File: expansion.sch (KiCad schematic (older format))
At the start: 3 parts, among them J7 DF40HC(3.5)-60DS, J9 DF40HC(3.5)-60DS, U1 IMX8MM

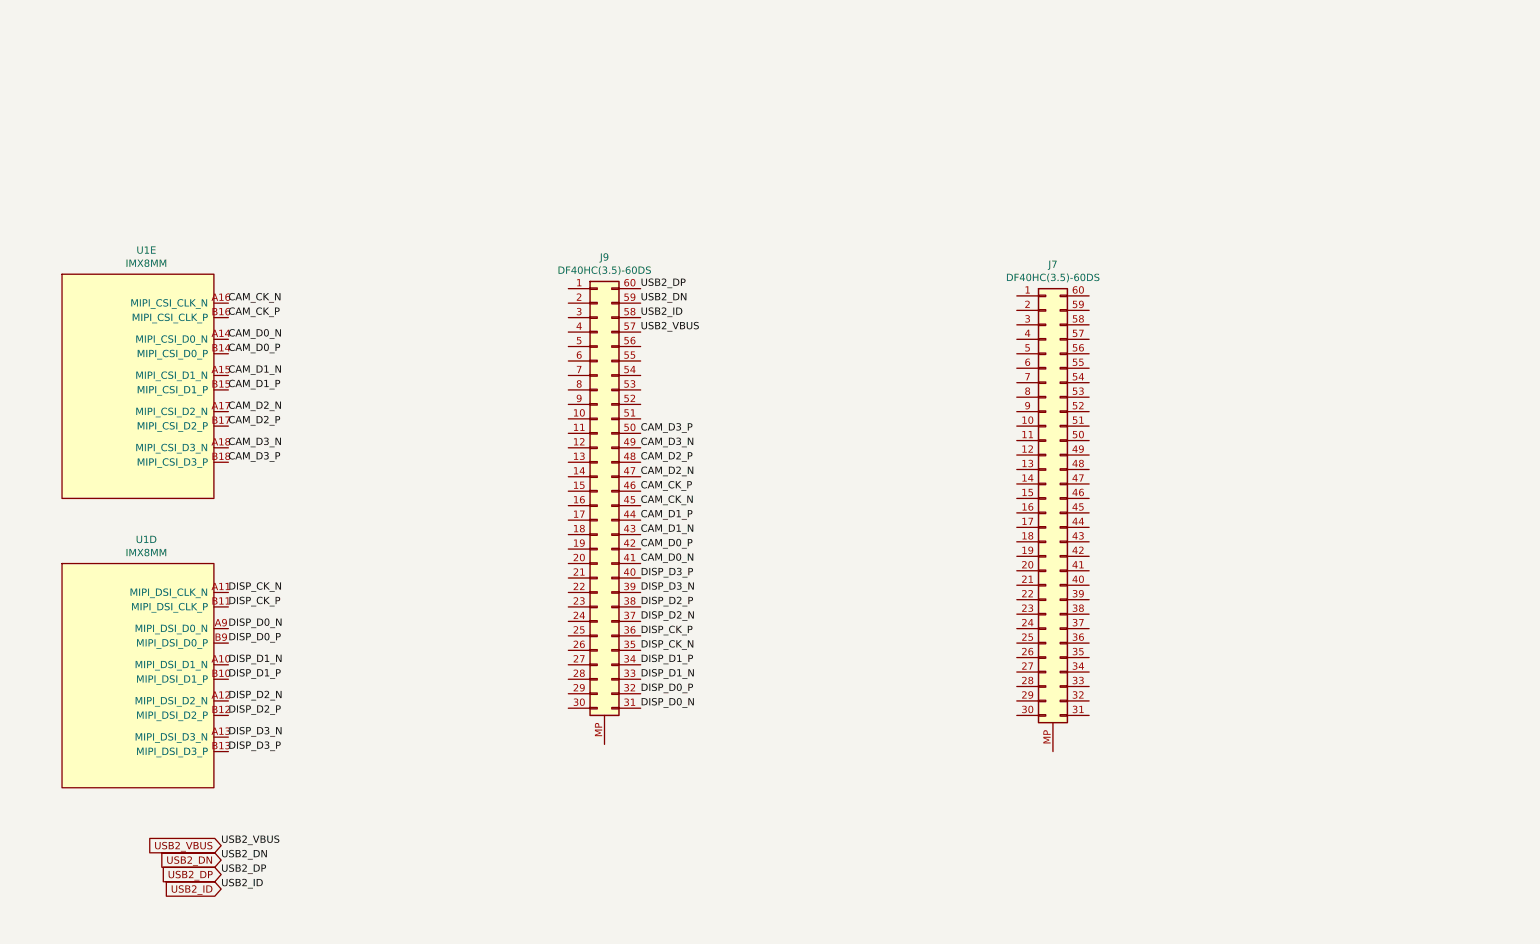
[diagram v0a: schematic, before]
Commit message: More new layout, buttons, and routing
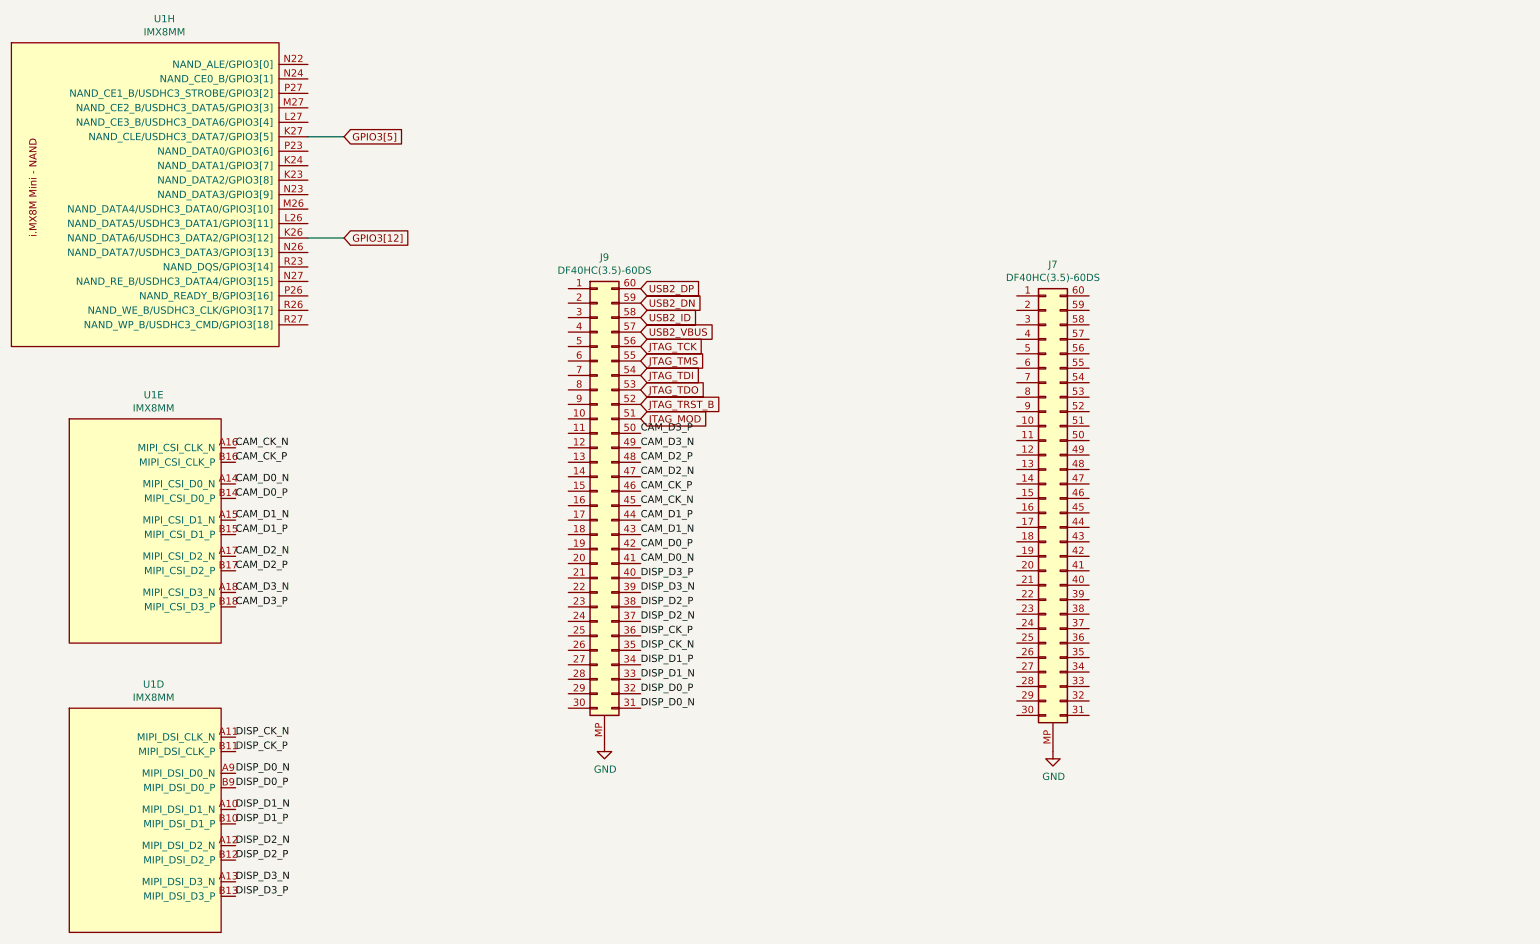
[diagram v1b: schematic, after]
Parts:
- added unit 8 of U1
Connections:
- net JTAG_MOD: now reaches J9.51 (Pin_51)
- net JTAG_TRST_B: now reaches J9.52 (Pin_52)
- net JTAG_TDO: now reaches J9.53 (Pin_53)
- net JTAG_TDI: now reaches J9.54 (Pin_54)
- net JTAG_TMS: now reaches J9.55 (Pin_55)
- net JTAG_TCK: now reaches J9.56 (Pin_56)
- net GND: now reaches J9.MP
- net GND: now also J7.MP
- new net GPIO3[12]: U1.K26 (NAND_DATA6/USDHC3_DATA2/GPIO3[12])
- new net GPIO3[5]: U1.K27 (NAND_CLE/USDHC3_DATA7/GPIO3[5])
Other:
- moved on the sheet: U1D, U1E
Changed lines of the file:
@@
 	1    0    0    -1
 $EndComp
-Text Label 2200 2650 0    50   ~ 0
+Text Label 2250 3650 0    50   ~ 0
 CAM_CK_N
-Text Label 2200 2750 0    50   ~ 0
+Text Label 2250 3750 0    50   ~ 0
 CAM_CK_P
-Text Label 2200 2900 0    50   ~ 0
+Text Label 2250 3900 0    50   ~ 0
 CAM_D0_N
-Text Label 2200 3000 0    50   ~ 0
+Text Label 2250 4000 0    50   ~ 0
 CAM_D0_P
-Text Label 2200 3150 0    50   ~ 0
+Text Label 2250 4150 0    50   ~ 0
 CAM_D1_N
-Text Label 2200 3250 0    50   ~ 0
+Text Label 2250 4250 0    50   ~ 0
 CAM_D1_P
 $Comp
 L mxenc:MIMX8MM6DVTLZAA U?
 U 5 1 5E38B0F0
-P 1600 5150
+P 1650 6150
 AR Path="/5DFA108C/5E38B0F0" Ref="U?"  Part="5"
 AR Path="/5E34BAA5/5E38B0F0" Ref="U1"  Part="5"
-F 0 "U1" H 1633 8015 50  0000 C CNN
-F 1 "IMX8MM" H 1633 7924 50  0000 C CNN
-F 2 "mxenc:BGA-729_27x27_14.0x14.0mm" H 1850 7900 50  0001 C CNN
-F 3 "" H 850 7900 50  0001 C CNN
-F 4 "NXP" H 1600 5150 50  0001 C CNN "Mfgr"
-F 5 "MIMX8MM6CVTKZAA" H 1600 5150 50  0001 C CNN "Part"
-F 6 "568-15276-ND" H 1600 5150 50  0001 C CNN "Vendorpart"
-	5    1600 5150
+F 0 "U1" H 1683 9015 50  0000 C CNN
+F 1 "IMX8MM" H 1683 8924 50  0000 C CNN
+F 2 "mxenc:BGA-729_27x27_14.0x14.0mm" H 1900 8900 50  0001 C CNN
+F 3 "" H 900 8900 50  0001 C CNN
+F 4 "NXP" H 1650 6150 50  0001 C CNN "Mfgr"
+F 5 "MIMX8MM6CVTKZAA" H 1650 6150 50  0001 C CNN "Part"
+F 6 "568-15276-ND" H 1650 6150 50  0001 C CNN "Vendorpart"
+	5    1650 6150
 	1    0    0    -1
 $EndComp
-Text Label 2200 3400 0    50   ~ 0
+Text Label 2250 4400 0    50   ~ 0
 CAM_D2_N
-Text Label 2200 3500 0    50   ~ 0
+Text Label 2250 4500 0    50   ~ 0
 CAM_D2_P
-Text Label 2200 3650 0    50   ~ 0
+Text Label 2250 4650 0    50   ~ 0
 CAM_D3_N
-Text Label 2200 3750 0    50   ~ 0
+Text Label 2250 4750 0    50   ~ 0
 CAM_D3_P
 Text Label 5050 4050 0    50   ~ 0
@@
 L mxenc:MIMX8MM6DVTLZAA U?
 U 4 1 5E3AB6A2
-P 1600 7150
+P 1650 8150
 AR Path="/5D6742B7/5E3AB6A2" Ref="U?"  Part="4"
 AR Path="/5E34BAA5/5E3AB6A2" Ref="U1"  Part="4"
-F 0 "U1" H 1633 10015 50  0000 C CNN
-F 1 "IMX8MM" H 1633 9924 50  0000 C CNN
-F 2 "mxenc:BGA-729_27x27_14.0x14.0mm" H 1850 9900 50  0001 C CNN
-F 3 "" H 850 9900 50  0001 C CNN
-F 4 "NXP" H 1600 7150 50  0001 C CNN "Mfgr"
-F 5 "MIMX8MM6CVTKZAA" H 1600 7150 50  0001 C CNN "Part"
-F 6 "568-15276-ND" H 1600 7150 50  0001 C CNN "Vendorpart"
-	4    1600 7150
+F 0 "U1" H 1683 11015 50  0000 C CNN
+F 1 "IMX8MM" H 1683 10924 50  0000 C CNN
+F 2 "mxenc:BGA-729_27x27_14.0x14.0mm" H 1900 10900 50  0001 C CNN
+F 3 "" H 900 10900 50  0001 C CNN
+F 4 "NXP" H 1650 8150 50  0001 C CNN "Mfgr"
+F 5 "MIMX8MM6CVTKZAA" H 1650 8150 50  0001 C CNN "Part"
+F 6 "568-15276-ND" H 1650 8150 50  0001 C CNN "Vendorpart"
+	4    1650 8150
 	1    0    0    -1
 $EndComp
-Text Label 2200 4650 0    50   ~ 0
+Text Label 2250 5650 0    50   ~ 0
 DISP_CK_N
-Text Label 2200 4750 0    50   ~ 0
+Text Label 2250 5750 0    50   ~ 0
 DISP_CK_P
-Text Label 2200 4900 0    50   ~ 0
+Text Label 2250 5900 0    50   ~ 0
 DISP_D0_N
-Text Label 2200 5000 0    50   ~ 0
+Text Label 2250 6000 0    50   ~ 0
 DISP_D0_P
-Text Label 2200 5150 0    50   ~ 0
+Text Label 2250 6150 0    50   ~ 0
 DISP_D1_N
-Text Label 2200 5250 0    50   ~ 0
+Text Label 2250 6250 0    50   ~ 0
 DISP_D1_P
-Text Label 2200 5400 0    50   ~ 0
+Text Label 2250 6400 0    50   ~ 0
 DISP_D2_N
-Text Label 2200 5500 0    50   ~ 0
+Text Label 2250 6500 0    50   ~ 0
 DISP_D2_P
-Text Label 2200 5650 0    50   ~ 0
+Text Label 2250 6650 0    50   ~ 0
 DISP_D3_N
-Text Label 2200 5750 0    50   ~ 0
+Text Label 2250 6750 0    50   ~ 0
 DISP_D3_P
 Text Label 5050 5050 0    50   ~ 0
@@
 Text Label 5050 4550 0    50   ~ 0
 DISP_D3_P
-Text Label 2150 6400 0    50   ~ 0
+Text GLabel 5050 2850 2    50   Input ~ 0
 USB2_VBUS
-Text Label 2150 6500 0    50   ~ 0
+Text GLabel 5050 2650 2    50   Input ~ 0
 USB2_DN
-Text Label 2150 6600 0    50   ~ 0
+Text GLabel 5050 2550 2    50   Input ~ 0
 USB2_DP
-Text Label 2150 6700 0    50   ~ 0
+Text GLabel 5050 2750 2    50   Input ~ 0
 USB2_ID
-Text GLabel 2150 6400 0    50   Input ~ 0
-USB2_VBUS
-Text GLabel 2150 6500 0    50   Input ~ 0
-USB2_DN
-Text GLabel 2150 6600 0    50   Input ~ 0
-USB2_DP
-Text GLabel 2150 6700 0    50   Input ~ 0
-USB2_ID
-Text Label 5050 2650 0    50   ~ 0
-USB2_DN
-Text Label 5050 2550 0    50   ~ 0
-USB2_DP
-Text Label 5050 2850 0    50   ~ 0
-USB2_VBUS
-Text Label 5050 2750 0    50   ~ 0
-USB2_ID
+$Comp
+L power:GND #PWR0151
+U 1 1 5E62C901
+P 4800 5700
+F 0 "#PWR0151" H 4800 5450 50  0001 C CNN
+F 1 "GND" H 4805 5527 50  0000 C CNN
+F 2 "" H 4800 5700 50  0001 C CNN
+F 3 "" H 4800 5700 50  0001 C CNN
+	1    4800 5700
+	1    0    0    -1
+$EndComp
+$Comp
+L power:GND #PWR0152
+U 1 1 5E62D325
+P 7900 5750
+F 0 "#PWR0152" H 7900 5500 50  0001 C CNN
+F 1 "GND" H 7905 5577 50  0000 C CNN
+F 2 "" H 7900 5750 50  0001 C CNN
+F 3 "" H 7900 5750 50  0001 C CNN
+	1    7900 5750
+	1    0    0    -1
+$EndComp
+Text GLabel 5050 2950 2    50   Input ~ 0
+JTAG_TCK
+Text GLabel 5050 3050 2    50   Input ~ 0
+JTAG_TMS
+Text GLabel 5050 3150 2    50   Input ~ 0
+JTAG_TDI
+Text GLabel 5050 3250 2    50   Input ~ 0
+JTAG_TDO
+Text GLabel 5050 3350 2    50   Input ~ 0
+JTAG_TRST_B
+Text GLabel 5050 3450 2    50   Input ~ 0
+JTAG_MOD
+$Comp
+L mxenc:MIMX8MM6DVTLZAA U1
+U 8 1 5E66E0E3
+P 1650 3550
+F 0 "U1" H 1758 6415 50  0000 C CNN
+F 1 "IMX8MM" H 1758 6324 50  0000 C CNN
+F 2 "mxenc:BGA-729_27x27_14.0x14.0mm" H 1900 6300 50  0001 C CNN
+F 3 "" H 900 6300 50  0001 C CNN
+	8    1650 3550
+	1    0    0    -1
+$EndComp
+Text GLabel 3000 2200 2    50   Input ~ 0
+GPIO3[12]
+Wire Wire Line
+	3000 2200 2750 2200
+Wire Wire Line
+	3000 1500 2750 1500
+Text GLabel 3000 1500 2    50   Input ~ 0
+GPIO3[5]
 $EndSCHEMATC

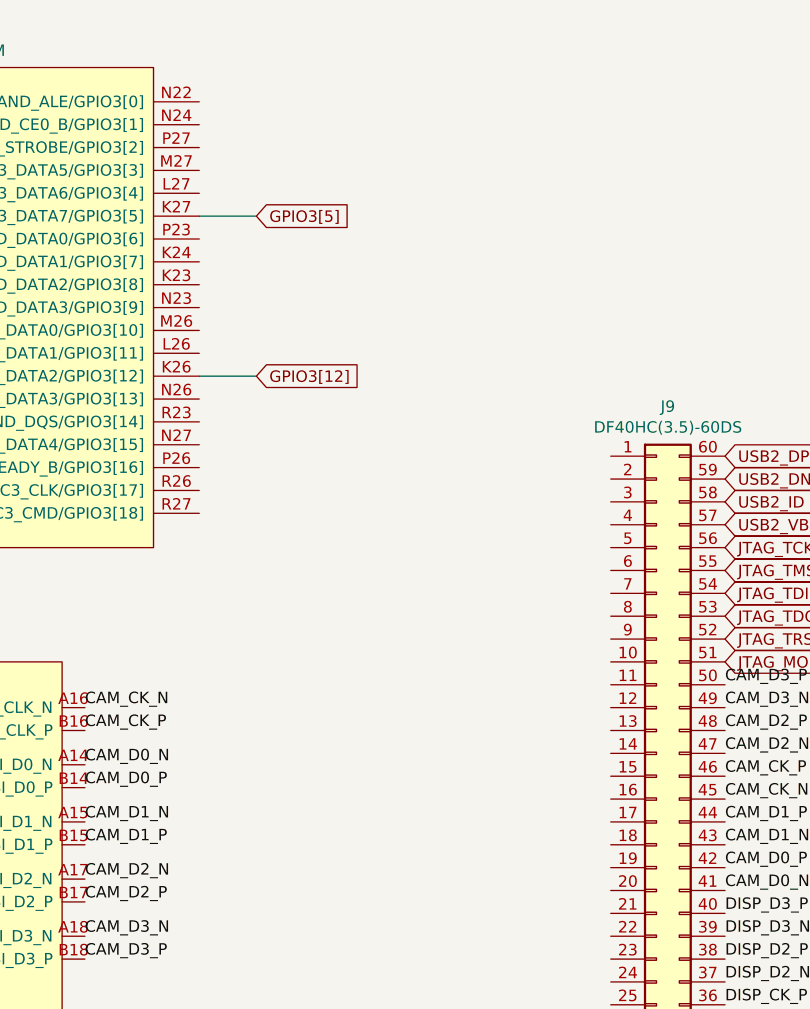
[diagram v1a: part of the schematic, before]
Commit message: rerouted sd, added some gpio, started power input
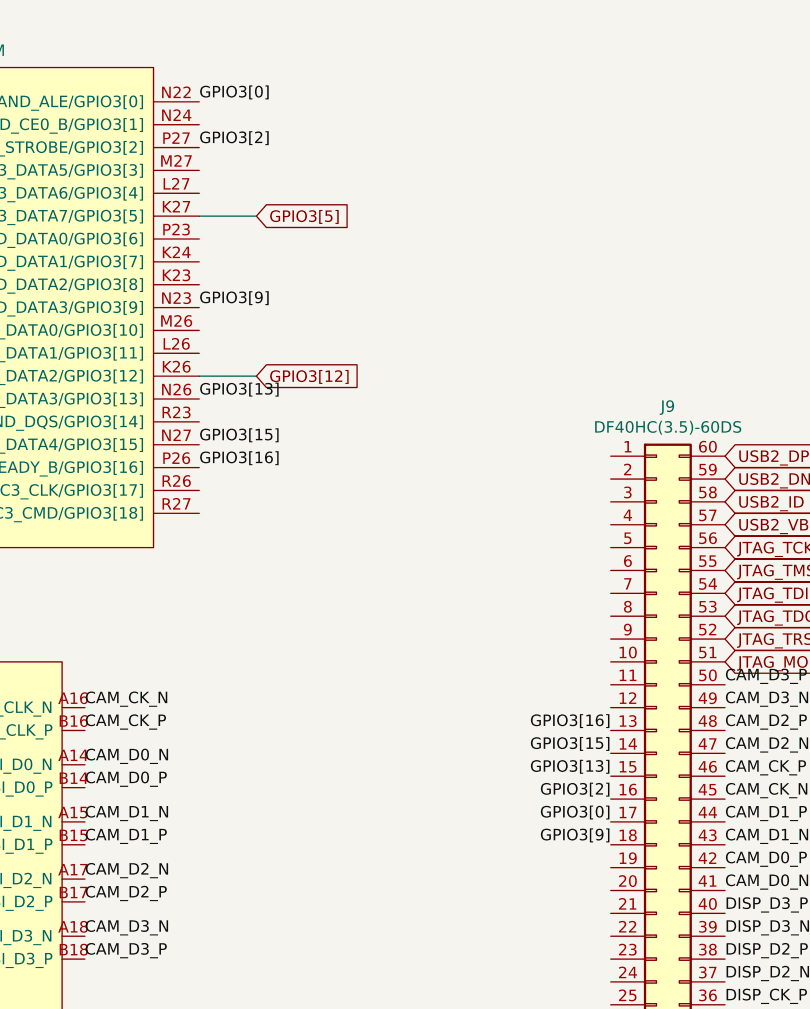
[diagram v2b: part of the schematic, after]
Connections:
- net GPIO3[16]: now reaches J9.13 (Pin_13)
- net GPIO3[16]: now also U1.P26 (NAND_READY_B/GPIO3[16])
- net GPIO3[15]: now reaches J9.14 (Pin_14)
- net GPIO3[15]: now also U1.N27 (NAND_RE_B/USDHC3_DATA4/GPIO3[15])
- net GPIO3[13]: now reaches J9.15 (Pin_15)
- net GPIO3[13]: now also U1.N26 (NAND_DATA7/USDHC3_DATA3/GPIO3[13])
- net GPIO3[2]: now reaches J9.16 (Pin_16)
- net GPIO3[2]: now also U1.P27 (NAND_CE1_B/USDHC3_STROBE/GPIO3[2])
- net GPIO3[0]: now reaches J9.17 (Pin_17)
- net GPIO3[0]: now also U1.N22 (NAND_ALE/GPIO3[0])
- net GPIO3[9]: now reaches J9.18 (Pin_18)
- net GPIO3[9]: now also U1.N23 (NAND_DATA3/GPIO3[9])
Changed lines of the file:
@@
 Text GLabel 3000 1500 2    50   Input ~ 0
 GPIO3[5]
+Text Label 2750 2300 0    50   ~ 0
+GPIO3[13]
+Text Label 2750 2500 0    50   ~ 0
+GPIO3[15]
+Text Label 2750 2600 0    50   ~ 0
+GPIO3[16]
+Text Label 2750 1200 0    50   ~ 0
+GPIO3[2]
+Text Label 2750 1000 0    50   ~ 0
+GPIO3[0]
+Text Label 2750 1900 0    50   ~ 0
+GPIO3[9]
+Text Label 4550 4150 2    50   ~ 0
+GPIO3[0]
+Text Label 4550 4250 2    50   ~ 0
+GPIO3[9]
+Text Label 4550 3950 2    50   ~ 0
+GPIO3[13]
+Text Label 4550 3850 2    50   ~ 0
+GPIO3[15]
+Text Label 4550 3750 2    50   ~ 0
+GPIO3[16]
+Text Label 4550 4050 2    50   ~ 0
+GPIO3[2]
 $EndSCHEMATC
